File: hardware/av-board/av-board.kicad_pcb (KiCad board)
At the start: 4 copper layers, 130 x 69.4 mm, 215 parts, among them J1 RCA Y, J10 2x20 socket, J2 RCA Pb, J3 RCA Pr, J4 RCA L, J5 RCA R, J6 HDMI-001, J9 2x20 socket, U1 ADV7842KBCZ-5, U10 TPD4E05U06DQAR, U2 ADV7511KSTZ, U3 PCM1808PWR, U4 TLV62569DBVR, U5 TPS7A7001DDAR, U6 TPS7A7001DDAR, U7 TPS7A7001DDAR, U8 TPD4E05U06DQAR, U9 TPD4E05U06DQAR, Y1 28.63636MHz 20pF

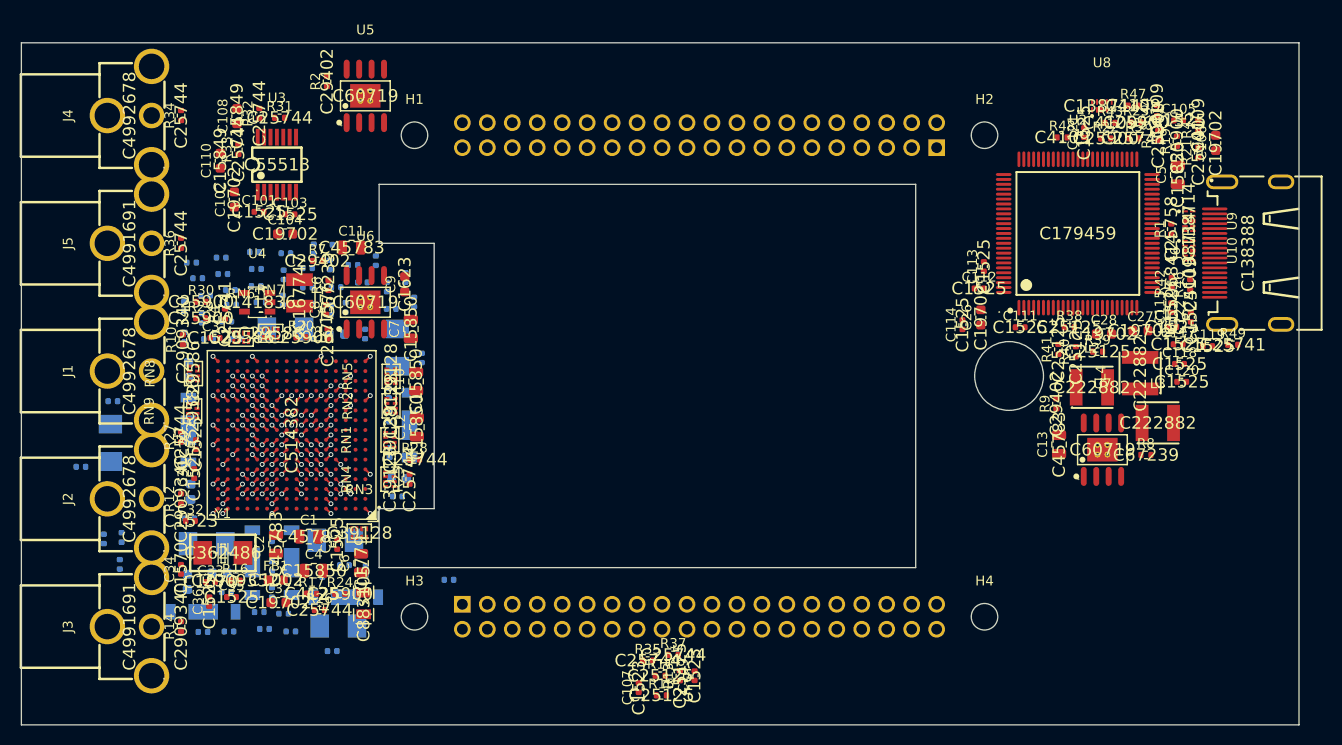
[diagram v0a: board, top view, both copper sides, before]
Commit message: Placement: parts by the pins they serve, both header buses flat
The router was failing on placement, not on routing time:

- Small parts were anchored on the first earlier IC sharing any net. Pull-ups to 3V3 went to
  the 3V3 regulator (R20-R25 near J9, 35-45 mm from their ADV7842 balls), and the 51 R
  video terminations (on TERM_x only, no IC pad) fell back to the middle of the bottom edge.
  Now a part on a signal goes to the IC pin it serves, else beside the part it hangs on, else
  the connector pin; supply nets do not count. The terminations sit at the ADV7842 (UG-214
  App. A), the ADV7511 audio series resistors at the source, J9 (HWG 7.3). Parts wait until
  what they hang on is placed.
- J10 had Y0-Y7 on its left pins while the 75 R arrays put out C0..C7 first: every line crossed
  every other in the 5 mm under the arrays. J10 is now in array order (LLC stays on the CLK
  pin: 2 crossings). J9 is in the ADV7511 pin order round the chip (0 crossings); its CLK is
  an output and leaves the header CLK pin. gen_pcb.py prints the crossings per bus.
- The PCM1808 I2S moves from J10 pins 23-26 (45 mm away) to J9 pins 37-40 (10 mm).
- The regulators move out of the band between J9 and the ADV7511 to the empty corner under it.

placecheck.py lists parts far from their nets; snap.py renders a board to PNG. design.md
pin tables follow. ERC clean, schematic = board.py on 897 pins.

Co-Authored-By: Claude Opus 5.5 <noreply@anthropic.com>
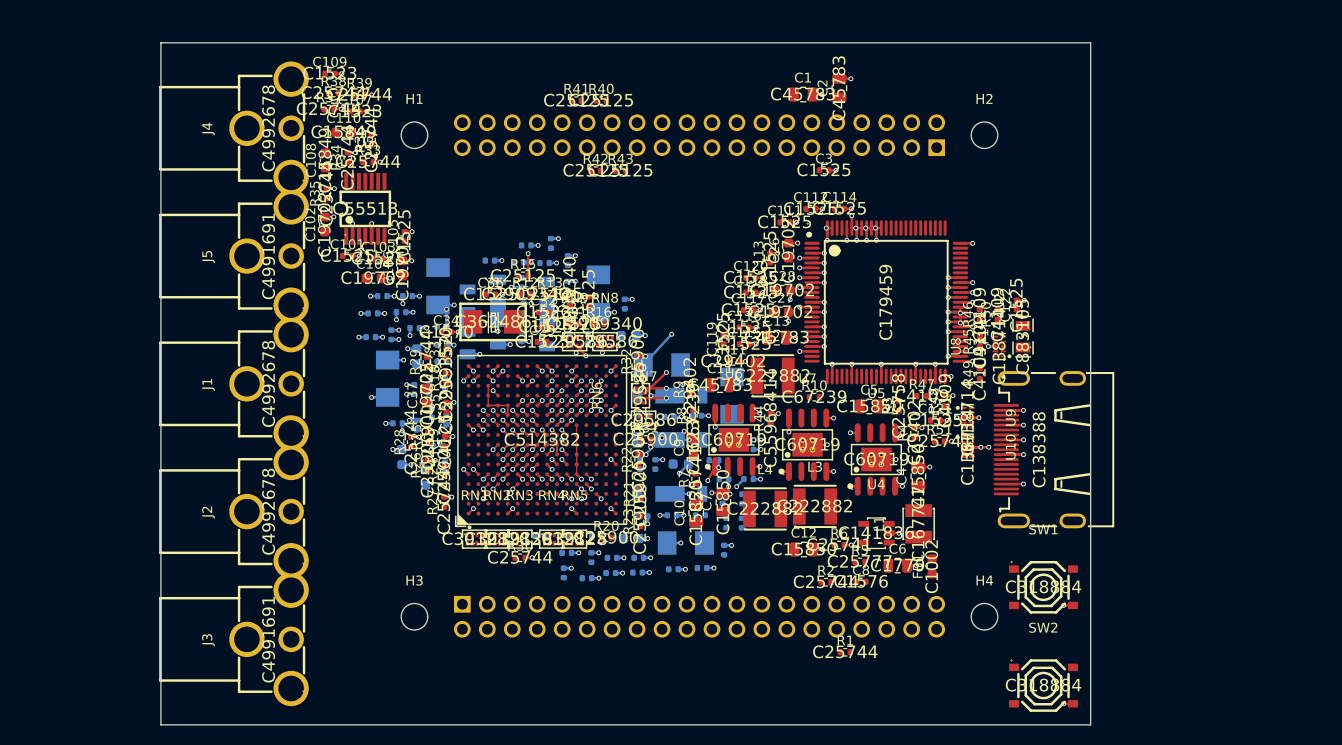
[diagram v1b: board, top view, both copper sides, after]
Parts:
- added R50: 2k, Resistor_SMD:R_0402_1005Metric, F.Cu at (159.3, 48.2)
- added R51: 100k, Resistor_SMD:R_0402_1005Metric, F.Cu at (153.4, 61.1)
- added SW1: TS-1187A-B-A-B, lcsc:SW-SMD_4P-L5.1-W5.1-P3.70-LS6.5-TL_H1.5, F.Cu at (164.0, 76.0)
- added SW2: TS-1187A-B-A-B, lcsc:SW-SMD_4P-L5.1-W5.1-P3.70-LS6.5-TL_H1.5, F.Cu at (164.0, 86.0)
- R1: value 169k -> 10k
- R10: value 24 -> 78.7k
- R11: value 51 -> 30.1k
- R16: value 390k -> 24
- R17: value 499 -> 51
- R18: value 4.7k -> 390k
- R19: value 4.7k -> 499
- R2: value 30.1k -> 10k
- R25, R26, R31, R32: value 10k -> 4.7k
- R29, R30: value 4.7k -> 10k
- R3: value 316k -> 169k
- R38, R39: value 51 -> 10k
- R4: value 100k -> 30.1k
- R42: value 887 -> 51
- R43: value 2k -> 51
- R44: value 2k -> 887
- R49: value 100k -> 2k
- R5: value 100k -> 316k
- R6: value 78.7k -> 100k
- R7: value 30.1k -> 100k
- moved C106 83.7 mm to (98.8, 43.6)
- moved R19 80.5 mm to (103.1, 61.2)
- moved C105 79.6 mm to (99.0, 40.3), turned to 90 degrees
- moved R39 79.5 mm to (94.4, 25.9)
- moved R38 78.6 mm to (91.8, 25.7)
- moved R18 76.5 mm to (103.2, 54.8)
- moved C2 73.8 mm to (143.2, 25.2)
- moved F1 72.4 mm to (161.9, 50.5)
- moved R2 71.9 mm to (141.9, 75.5), turned to 0 degrees
- moved C109 71.6 mm to (91.4, 23.7), turned to 0 degrees
- moved R4 71.2 mm to (150.9, 60.3)
- moved C1 67.5 mm to (139.6, 25.9)
- moved L1 67.2 mm to (151.3, 69.5)
- moved U4 67.2 mm to (147.0, 70.5)
- moved FB1 66.8 mm to (152.7, 73.9), turned to 90 degrees
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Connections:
- net TMDS_CKN renamed TMDS_CK_N
- net TMDS_CKP renamed TMDS_CK_P
- net TMDS_D0N renamed TMDS_D0_N
- net TMDS_D0P renamed TMDS_D0_P
- net TMDS_D1N renamed TMDS_D1_N
- net TMDS_D1P renamed TMDS_D1_P
- net TMDS_D2N renamed TMDS_D2_N
- net TMDS_D2P renamed TMDS_D2_P
- J10 pad 1: IN_Y0 -> IN_C0
- J10 pad 13: IN_C5 -> IN_C7
- J10 pad 14: IN_C4 -> IN_Y0
- J10 pad 15: IN_C3 -> IN_Y1
- J10 pad 16: IN_C2 -> IN_Y2
- J10 pad 17: IN_C1 -> IN_Y3
- J10 pad 18: IN_C0 -> IN_Y4
- J10 pad 19: IN_HS -> IN_Y5
- J10 pad 2: IN_Y1 -> IN_C1
- J10 pad 21: IN_VS -> IN_Y6
- J10 pad 22: IN_DE -> IN_Y7
- J10 pad 23: IN_SCKI -> IN_SCL
- J10 pad 24: IN_BCK -> IN_INT1
- J10 pad 25: IN_LRCK -> IN_SDA
- J10 pad 26: IN_DOUT -> IN_RESET_N
- J10 pad 27: IN_SCL -> GND
- J10 pad 28: IN_SDA -> GND
- J10 pad 29: IN_RESET_N -> GND
- J10 pad 3: IN_Y2 -> IN_C2
- J10 pad 30: IN_INT1 -> GND
- J10 pad 31: GND -> IN_KEY1
- J10 pad 32: GND -> IN_KEY2
- J10 pad 4: IN_Y3 -> IN_C3
- J10 pad 5: IN_Y4 -> IN_VS
- J10 pad 6: IN_Y5 -> IN_HS
- J10 pad 7: IN_Y6 -> IN_C4
- J10 pad 8: IN_Y7 -> IN_C5
- J10 pad 9: IN_C7 -> IN_DE
- J9 pad 1: OUT_Y0 -> OUT_PD
- J9 pad 10: OUT_C6 -> OUT_C2
- J9 pad 13: OUT_C5 -> OUT_C1
- J9 pad 14: OUT_C4 -> OUT_CLK
- J9 pad 15: OUT_C3 -> OUT_C0
- J9 pad 16: OUT_C2 -> OUT_Y7
- J9 pad 17: OUT_C1 -> OUT_Y6
- J9 pad 18: OUT_C0 -> OUT_Y5
- J9 pad 19: OUT_HSYNC -> OUT_Y4
- J9 pad 2: OUT_Y1 -> OUT_INT
- J9 pad 20: OUT_CLK -> OUT_Y3
- J9 pad 21: OUT_VSYNC -> OUT_Y2
- J9 pad 22: OUT_DE -> OUT_Y1
- J9 pad 23: OUT_MCLK -> OUT_Y0
- J9 pad 24: OUT_SCLK -> OUT_DE
- J9 pad 25: OUT_LRCLK -> OUT_HSYNC
- J9 pad 26: OUT_I2S0 -> OUT_VSYNC
- J9 pad 27: OUT_SCL -> OUT_MCLK
- J9 pad 28: OUT_SDA -> OUT_I2S0
- J9 pad 29: OUT_INT -> OUT_SCLK
- J9 pad 3: OUT_Y2 -> OUT_SCL
- J9 pad 30: OUT_PD -> OUT_LRCLK
- J9 pad 37: GND -> IN_SCKI
- J9 pad 38: GND -> IN_LRCK
- J9 pad 39: GND -> IN_DOUT
- J9 pad 4: OUT_Y3 -> OUT_SDA
- J9 pad 40: GND -> IN_BCK
- J9 pad 5: OUT_Y4 -> OUT_C7
- J9 pad 6: OUT_Y5 -> OUT_C6
- J9 pad 7: OUT_Y6 -> OUT_C5
- J9 pad 8: OUT_Y7 -> OUT_C4
- J9 pad 9: OUT_C7 -> OUT_C3
- R1 pad 2: FB_3V3 -> IN_KEY1
- R10 pad 1: RCA_Y -> 1V8B
- R10 pad 2: TERM_Y -> FB_1V8B
- R11 pad 1: TERM_Y -> FB_1V8B
- R12 pad 1: RCA_PB -> RCA_Y
- R12 pad 2: TERM_PB -> TERM_Y
- R13 pad 1: TERM_PB -> TERM_Y
- R14 pad 1: RCA_PR -> RCA_PB
- R14 pad 2: TERM_PR -> TERM_PB
- R15 pad 1: TERM_PR -> TERM_PB
- R16 pad 1: XTALP -> RCA_PR
- R16 pad 2: XTALN -> TERM_PR
- R17 pad 1: RTERM -> TERM_PR
- R18 pad 1: 3V3 -> XTALP
- R18 pad 2: IN_SCL -> XTALN
- R19 pad 1: 3V3 -> RTERM
- R19 pad 2: IN_SDA -> GND
- R2 pad 1: FB_3V3 -> 3V3
- R2 pad 2: GND -> IN_KEY2
- R20 pad 1: IN_RESET_N -> 3V3
- R20 pad 2: GND -> IN_SCL
- R21 pad 2: IN_INT1 -> IN_SDA
- R22 pad 1: 3V3 -> IN_RESET_N
- R22 pad 2: PWRDN1 -> GND
- R23 pad 2: TEST8 -> IN_INT1
- R24 pad 1: TEST8 -> 3V3
- R24 pad 2: GND -> PWRDN1
- R25 pad 1: PD_DDCB_SCL -> 3V3
- R25 pad 2: GND -> TEST8
- R26 pad 1: PD_DDCA_SCL -> TEST8
- R27 pad 1: PD_VGA_SCL -> PD_DDCB_SCL
- R28 pad 1: PD_TTX_SCL -> PD_DDCA_SCL
- R29 pad 1: PD_SDRAM_LDQS -> PD_VGA_SCL
- R3 pad 1: 2V5 -> 3V3
- R3 pad 2: FB_2V5 -> FB_3V3
- R30 pad 1: PD_SDRAM_UDQS -> PD_TTX_SCL
- R31 pad 1: MD0 -> PD_SDRAM_LDQS
- R32 pad 1: MD1 -> PD_SDRAM_UDQS
- R33 pad 1: FMT -> MD0
- R34 pad 1: RCA_L -> MD1
- R34 pad 2: AUD_DIV_L -> GND
- R35 pad 1: AUD_DIV_L -> FMT
- R36 pad 1: RCA_R -> RCA_L
- R36 pad 2: AUD_DIV_R -> AUD_DIV_L
- R37 pad 1: AUD_DIV_R -> AUD_DIV_L
- R38 pad 1: OUT_MCLK -> RCA_R
- R38 pad 2: TX_MCLK -> AUD_DIV_R
- R39 pad 1: OUT_SCLK -> AUD_DIV_R
- R39 pad 2: TX_SCLK -> GND
- R4 pad 1: FB_2V5 -> FB_3V3
- R40 pad 1: OUT_LRCLK -> OUT_MCLK
- R40 pad 2: TX_LRCLK -> TX_MCLK
- R41 pad 1: OUT_I2S0 -> OUT_SCLK
- R41 pad 2: TX_I2S0 -> TX_SCLK
- R42 pad 1: R_EXT -> OUT_LRCLK
- R42 pad 2: GND -> TX_LRCLK
- R43 pad 1: 3V3 -> OUT_I2S0
- R43 pad 2: OUT_SCL -> TX_I2S0
- R44 pad 1: 3V3 -> R_EXT
- R44 pad 2: OUT_SDA -> GND
- R45 pad 2: OUT_INT -> OUT_SCL
- R46 pad 1: OUT_PD -> 3V3
- R46 pad 2: GND -> OUT_SDA
- R47 pad 1: HDMI_5V -> 3V3
- R47 pad 2: HDMI_SCL -> OUT_INT
- R48 pad 1: HDMI_5V -> OUT_PD
- R48 pad 2: HDMI_SDA -> GND
- R49 pad 1: HDMI_HPD -> HDMI_5V
- R49 pad 2: GND -> HDMI_SCL
- R5 pad 1: 3V3 -> 2V5
- R5 pad 2: EN_1V8 -> FB_2V5
- R6 pad 1: 1V8A -> FB_2V5
- R6 pad 2: FB_1V8A -> GND
- R7 pad 1: FB_1V8A -> 3V3
- R7 pad 2: GND -> EN_1V8
- R8 pad 1: 1V8B -> 1V8A
- R8 pad 2: FB_1V8B -> FB_1V8A
- R9 pad 1: FB_1V8B -> FB_1V8A
- RN1 pad 1: AV_Y0 -> AV_C0
- RN1 pad 2: AV_Y1 -> AV_C1
- RN1 pad 3: AV_Y2 -> AV_C2
- RN1 pad 4: AV_Y3 -> AV_C3
- RN1 pad 5: IN_Y3 -> IN_C3
- RN1 pad 6: IN_Y2 -> IN_C2
- RN1 pad 7: IN_Y1 -> IN_C1
- RN1 pad 8: IN_Y0 -> IN_C0
- RN2 pad 1: AV_Y4 -> AV_VS
- RN2 pad 2: AV_Y5 -> AV_HS
- RN2 pad 3: AV_Y6 -> AV_C4
- RN2 pad 4: AV_Y7 -> AV_C5
- RN2 pad 5: IN_Y7 -> IN_C5
- RN2 pad 6: IN_Y6 -> IN_C4
- RN2 pad 7: IN_Y5 -> IN_HS
- RN2 pad 8: IN_Y4 -> IN_VS
- RN3 pad 1: AV_C0 -> AV_DE
- RN3 pad 2: AV_C1 -> AV_C6
- RN3 pad 3: AV_C2 -> AV_C7
- RN3 pad 4: AV_C3 -> AV_Y0
- RN3 pad 5: IN_C3 -> IN_Y0
- RN3 pad 6: IN_C2 -> IN_C7
- RN3 pad 7: IN_C1 -> IN_C6
- RN3 pad 8: IN_C0 -> IN_DE
- RN4 pad 1: AV_C4 -> AV_Y1
- RN4 pad 2: AV_C5 -> AV_Y2
- RN4 pad 3: AV_C6 -> AV_Y3
- RN4 pad 4: AV_C7 -> AV_Y4
- RN4 pad 5: IN_C7 -> IN_Y4
- RN4 pad 6: IN_C6 -> IN_Y3
- RN4 pad 7: IN_C5 -> IN_Y2
- RN4 pad 8: IN_C4 -> IN_Y1
- RN5 pad 1: AV_LLC -> AV_Y5
- RN5 pad 2: AV_HS -> AV_Y6
- RN5 pad 3: AV_VS -> AV_Y7
- RN5 pad 4: AV_DE -> AV_LLC
- RN5 pad 5: IN_DE -> IN_LLC
- RN5 pad 6: IN_VS -> IN_Y7
- RN5 pad 7: IN_HS -> IN_Y6
- RN5 pad 8: IN_LLC -> IN_Y5
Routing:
- net GND: track 41.7 -> 257.5 mm, vias 59 -> 266
- net AV_TVDD: track 2.83 -> 14.1 mm, vias 4 -> 17
- net AV_DVDDIO: track 8.49 -> 11.7 mm, vias 12 -> 9
- net AV_AVDD: track 4.24 -> 6.06 mm, vias 6 -> 8
- net AV_CVDD: track 4.24 -> 5.71 mm, vias 6 -> 1
- net +5V: track 1.41 -> 0.00 mm, vias 2 -> 0
- net AV_PVDD: track 1.41 -> 2.66 mm, vias 2 -> 3
- net AV_VDD: track 6.36 -> 7.42 mm
- added copper zone on In2.Cu, net AV_PVDD
- added copper zone on In2.Cu, net AV_TVDD
- removed copper zone on In2.Cu, net AV_CVDD
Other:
- board size 130 x 69.4 mm -> 94.6 x 69.4 mm

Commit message: Rail planes sized for their caps: 68 of 69 ADV7842 rail caps over their plane
40 of the ADV7842 rail caps sat off their planes (median 7 mm, up to 12 mm from their rail),
among them 10 per-ball 10/100 nF caps and AVDD/PVDD caps: noise on the ADC and PLL supplies,
and one more routed connection each into the crowd round the BGA.

- The planes widen past the BGA to hold their filter and every cap: AVDD over the top right,
  PVDD over the top left (taking room TVDD did not use), VDD and DVDDIO to the right with
  DVDDIO (25 caps per UG-214 Fig. 179) taking the larger lower part, up to the regulators.
- CVDD's filter and tantalum move from the right of the BGA, where they took VDD/DVDDIO room,
  to its left, four rows from the CVDD balls (C12-E12), in TVDD's spare room.
- The regulators move right, off the planes; U5/U4 spread so the buck has room.
- 10 uF rail caps go by their filter with the 33 uF ones (they are bulk), not round-robin on
  the balls under the BGA's edge.
- Bias resistors (RTERM, R_EXT), the REFP/REFN caps and the regulators' feedback dividers are
  placed before the decoupling, at their pins; the crystal moves 3 mm left, off E15/E16.
- The SDRAM pull-down arrays lose their first-place rank (meant for the 75 R arrays), so the
  analog input caps get the BGA's top edge.
- The PCM1808 VCC ferrite is written down with the PCM1808, so it sits there (was 65 mm away).

PCB=path makes a trial board elsewhere. ERC clean, schematic = board.py (897 pins), DRC: only
the unrouted connections.

Co-Authored-By: Claude Opus 5.5 <noreply@anthropic.com>
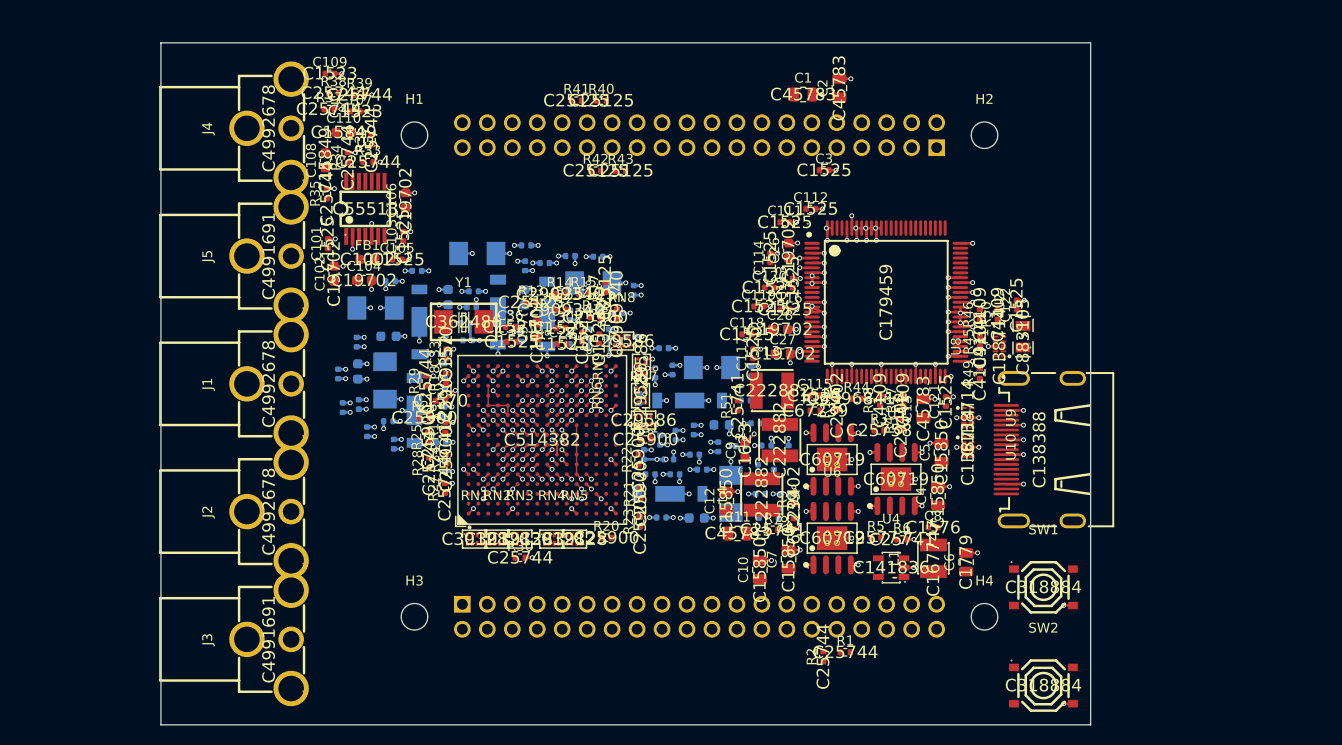
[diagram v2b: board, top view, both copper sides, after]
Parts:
- moved FB1 65.4 mm to (95.2, 42.6), turned to 0 degrees
- moved C18 35.3 mm to (97.0, 55.0)
- moved C98 26.1 mm to (138.1, 62.1)
- moved FL3 26.0 mm to (100.0, 58.0), turned to 90 degrees
- moved R51 20.8 mm to (132.9, 57.5), turned to 90 degrees
- moved C95 20.6 mm to (137.1, 68.5), turned to 90 degrees
- moved C70 19.4 mm to (122.8, 54.2), turned to 90 degrees
- moved C89 18.4 mm to (135.2, 66.5), turned to 0 degrees
- moved C91 18.3 mm to (135.0, 64.0), turned to 90 degrees
- moved C13 16.6 mm to (151.8, 57.8), turned to 90 degrees
- moved C88 16.6 mm to (133.1, 61.6)
- moved C69 16.0 mm to (122.9, 56.8), turned to 90 degrees
- moved C47 15.6 mm to (100.2, 43.8)
- moved C87 15.6 mm to (130.9, 61.7), turned to 90 degrees
- moved R9 15.3 mm to (138.6, 67.0)
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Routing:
- net AV_DVDDIO: track 11.7 -> 25.6 mm, vias 9 -> 25
- net GND: track 257.5 -> 243.9 mm, vias 266 -> 269
- net AV_AVDD: track 6.06 -> 15.6 mm, vias 8 -> 18
- net AV_VDD: track 7.42 -> 11.2 mm, vias 9 -> 13
- net AV_PVDD: track 2.66 -> 6.15 mm, vias 3 -> 7
- net AV_TVDD: track 14.1 -> 15.5 mm, vias 17 -> 19
